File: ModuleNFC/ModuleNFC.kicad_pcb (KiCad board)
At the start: 2 copper layers, 40 parts, among them J1 Conn_01x10_Male, J2 Conn_01x04_Male, J3 Conn_01x08_Male, J4 Conn_Coaxial, Q1 2N7002DM, SW1 SW_DIP_x02, U1 PN5321A3HN_C1xx, Y1 27.12MHz

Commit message: Esquemático y PCB versión 1
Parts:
- Y1: footprint Crystal:Crystal_SMD_0603-4Pin_6.0x3.5mm -> Crystal:Crystal_SMD_0603-2Pin_6.0x3.5mm
- moved C1 70.3 mm to (188.8, 64.2), turned to 180 degrees
- moved J4 63.2 mm to (213.5, 77.0)
- moved J3 61.6 mm to (182.9, 59.5), turned to 90 degrees
- moved C8 56.9 mm to (182.5, 72.9), turned to 90 degrees
- moved C13 56.3 mm to (206.5, 79.5), turned to 270 degrees
- moved L1 56.2 mm to (202.0, 80.5), turned to 180 degrees
- moved C9 56.1 mm to (191.5, 82.0), turned to 270 degrees
- moved C7 55.1 mm to (194.0, 79.0)
- moved C5 54.9 mm to (194.0, 75.0)
- moved C18 54.7 mm to (197.8, 70.2), turned to 270 degrees
- moved C10 54.3 mm to (193.5, 82.0), turned to 270 degrees
- moved R6 54.2 mm to (193.9, 70.2), turned to 270 degrees
- moved U1 50.2 mm to (187.0, 76.5), turned to 180 degrees
- moved C11 48.4 mm to (201.0, 77.0), turned to 90 degrees
- moved R7 48.0 mm to (199.7, 70.2), turned to 270 degrees
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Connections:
- J3 pad 1: /RSTOUTN -> Net-(J3-Pad1)
- J3 pad 3: GND -> Net-(J3-Pad3)
- J3 pad 4: +3V3 -> Net-(J3-Pad4)
- J3 pad 5: Net-(J3-Pad5) -> +3V3
- J3 pad 6: Net-(J3-Pad6) -> GND
- J3 pad 8: Net-(J3-Pad8) -> /RSTOUTN
- R10 pad 1: Net-(J3-Pad6) -> Net-(J3-Pad3)
- R11 pad 1: Net-(J3-Pad5) -> Net-(J3-Pad4)
- R12 pad 1: Net-(J3-Pad2) -> Net-(J3-Pad7)
- R8 pad 1: Net-(J3-Pad8) -> Net-(J3-Pad1)
- R9 pad 1: Net-(J3-Pad7) -> Net-(J3-Pad2)
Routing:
- net GND: track 0.00 -> 217.3 mm, vias 0 -> 5
- net +3V3: track 0.00 -> 148.3 mm, vias 0 -> 3
- net Net-(R1-Pad1): track 0.00 -> 56.6 mm, vias 0 -> 2
- net Net-(R2-Pad1): track 0.00 -> 43.3 mm, vias 0 -> 2
- net /MOSI_SDA_TX: track 0.00 -> 33.3 mm, vias 0 -> 3
- net /RSTOUTN: track 0.00 -> 29.7 mm, vias 0 -> 2
- net /NSS_SCL_RX: track 0.00 -> 28.7 mm, vias 0 -> 2
- net /AUX1: track 0.00 -> 28.2 mm, vias 0 -> 1
- net /AUX2: track 0.00 -> 23.7 mm, vias 0 -> 1
- net /SCK: track 0.00 -> 18.2 mm, vias 0 -> 2
- net Net-(C11-Pad1): track 0.00 -> 17.1 mm
- net /MISO: track 0.00 -> 17.0 mm, vias 0 -> 2
- net Net-(C18-Pad2): track 0.00 -> 16.6 mm
- net /DBG_RX: track 0.00 -> 14.1 mm, vias 0 -> 1
- net Net-(J3-Pad7): track 0.00 -> 14.0 mm
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
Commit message: Board modificaed
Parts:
- moved J4 59.7 mm to (167.7, 115.3), turned to 270 degrees
- moved C15 53.7 mm to (165.7, 110.8), turned to 180 degrees
- moved C16 53.2 mm to (169.7, 110.8), turned to 180 degrees
- moved C13 50.4 mm to (165.2, 108.3), turned to 180 degrees
- moved C14 49.6 mm to (170.2, 108.3), turned to 0 degrees
- moved C18 47.0 mm to (159.0, 96.8), turned to 180 degrees
- moved C2 45.9 mm to (148.2, 96.4)
- moved C1 45.9 mm to (152.7, 92.6)
- moved C10 45.9 mm to (157.4, 110.4)
- moved C4 45.9 mm to (153.4, 110.4)
- moved C5 45.9 mm to (157.9, 103.4)
- moved C6 45.9 mm to (157.9, 105.4)
- moved C7 45.9 mm to (157.9, 107.4)
- moved C8 45.9 mm to (146.4, 101.3)
- moved C9 45.9 mm to (155.4, 110.4)
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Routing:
- net /TX2: track 12.1 -> 22.5 mm
- net Net-(C18-Pad2): track 16.6 -> 8.33 mm
- net /TX1: track 12.3 -> 16.3 mm
- net +3V3: track 148.3 -> 150.9 mm
- net GND: track 217.3 -> 214.8 mm, vias 5 -> 3
- net Net-(C17-Pad1): track 7.98 -> 9.91 mm
- net Net-(C11-Pad1): track 17.1 -> 15.8 mm
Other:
- board outline added: 52 x 39 mm
- board text added: "KiCad E.D.A"

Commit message: Added dimensions
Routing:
- net GND: track 214.8 -> 212.0 mm

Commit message: Added comment at margin with parameters of PCB
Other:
- board text added: "* No se tiene restricciones sobre el tamaño de pistas. * Se utilizo las capacidades de fabricación nacional (Mayer). * La capacidad de Mayer planteada para este módulo fue 10 mils * La grilla utilizada para acomodar componente cómo primera aproximación fue 1mm * La grilla utilizada para routear las pistas varió entre 0.25 a 0.1mm"

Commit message: Add model 3D of PN532
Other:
- board text added: "KiCad E.D.A IND. ARG"
- board text added: "V1"
- board text removed: "KiCad E.D.A"

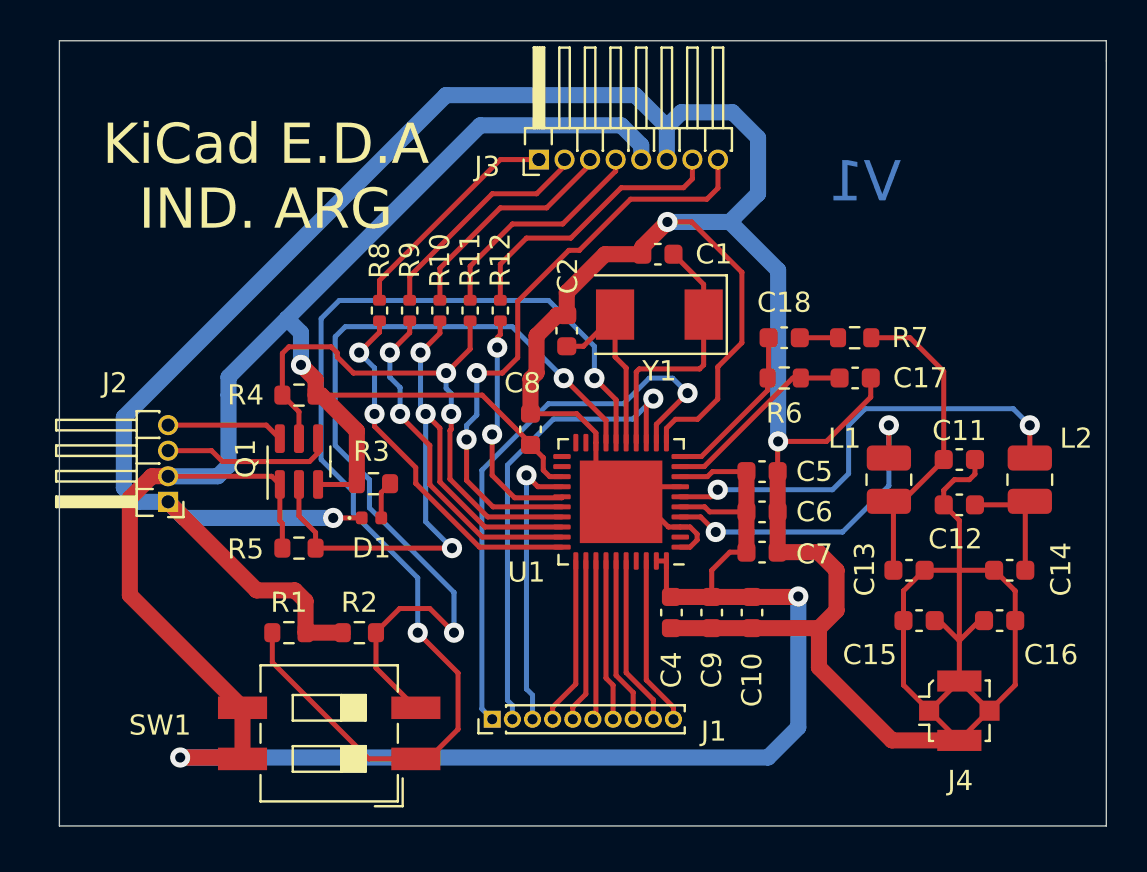
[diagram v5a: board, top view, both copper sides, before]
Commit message: Modification on PCB and Schematic on base of correction
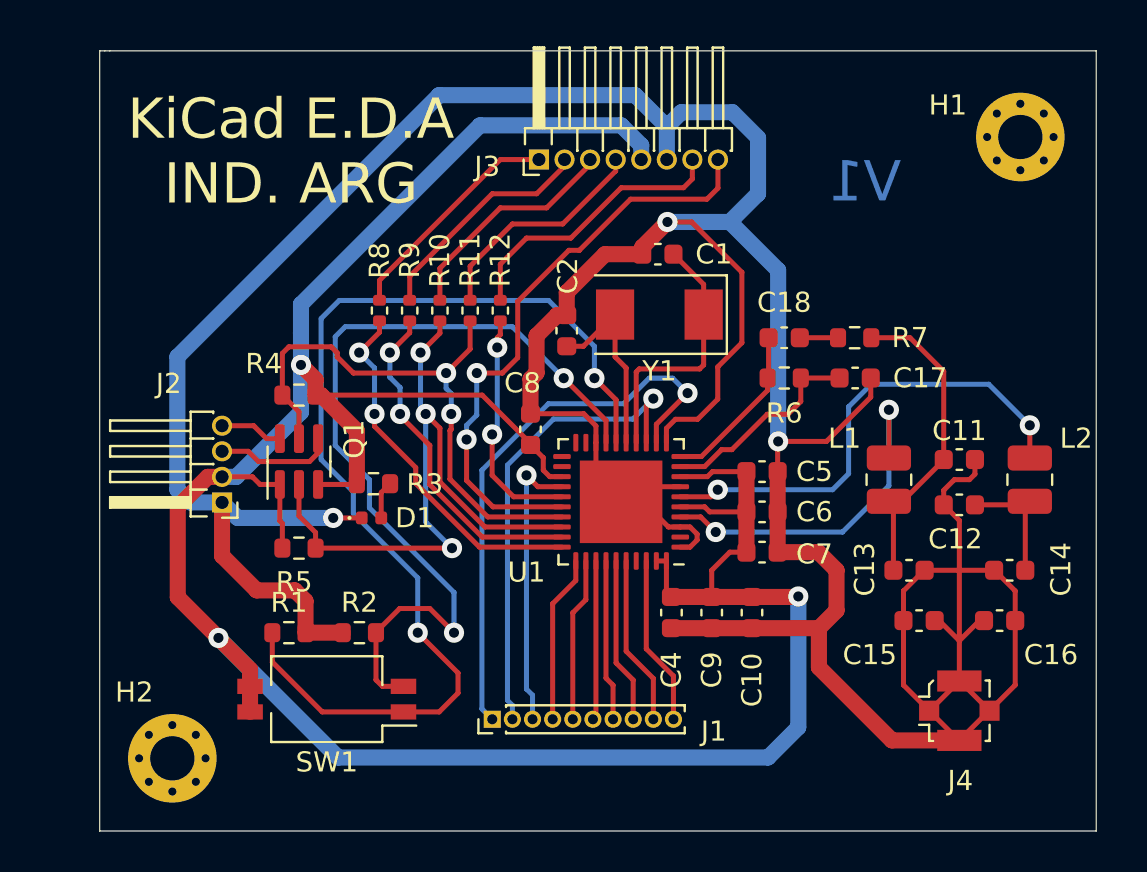
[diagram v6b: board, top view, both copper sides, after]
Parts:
- added H1: MountingHole, MountingHole:MountingHole_2.2mm_M2_Pad_Via, F.Cu at (170.7, 86.8)
- added H2: MountingHole, MountingHole:MountingHole_2.2mm_M2_Pad_Via, F.Cu at (128.6, 117.6)
- D1: value BLUE -> Led blue
- SW1: footprint Button_Switch_SMD:SW_DIP_SPSTx02_Slide_6.7x6.64mm_W8.61mm_P2.54mm_LowProfile -> Button_Switch_SMD:SW_DIP_SPSTx02_Slide_KingTek_DSHP02TS_W7.62mm_P1.27mm
- moved J2 2.68 mm to (131.1, 104.9)
- moved SW1 1.70 mm to (136.3, 114.7)
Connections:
- net /TX1 renamed Net-(L1-Pad2)
- net /TX2 renamed Net-(L2-Pad2)
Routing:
- net +3V3: track 150.9 -> 137.8 mm
- net GND: track 212.0 -> 207.6 mm
- net Net-(R1-Pad1): track 56.6 -> 53.6 mm
- net /SCL: track 5.83 -> 3.14 mm
- net /SDA: track 8.56 -> 5.87 mm
- net Net-(L2-Pad2): track 22.5 -> 24.1 mm
- net Net-(L1-Pad2): track 16.3 -> 17.8 mm
- net Net-(R2-Pad1): track 43.3 -> 42.6 mm
- net Net-(C17-Pad1): track 9.91 -> 10.6 mm
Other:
- board size 52 x 39 mm -> 49.5 x 38.8 mm
- board text added: "* No se tiene restricciones sobre el tamaño de pistas. * Se utilizo las capacidades de fabricación nacional (Mayer). * La capacidad de Mayer planteada para este módulo fue 10 mils * La grilla utilizada para acomodar componente cómo primera aproximación fue 1mm * La grilla utilizada para routear las pistas fue 0.1mm"
- board text removed: "* No se tiene restricciones sobre el tamaño de pistas. * Se utilizo las capacidades de fabricación nacional (Mayer). * La capacidad de Mayer planteada para este módulo fue 10 mils * La grilla utilizada para acomodar componente cómo primera aproximación fue 1mm * La grilla utilizada para routear las pistas varió entre 0.25 a 0.1mm"

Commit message: All modification with correction
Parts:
- added FID1: Fiducial, Fiducial:Fiducial_1mm_Mask2mm, F.Cu at (128.0, 119.1)
- added FID2: Fiducial, Fiducial:Fiducial_1mm_Mask2mm, F.Cu at (172.2, 119.1)
- added FID3: Fiducial, Fiducial:Fiducial_1mm_Mask2mm, F.Cu at (172.2, 85.6)
- C1, C10, C11, C12, C13, C14, C15, C16, C17, C18, C2, C4, C5, C6, C7, C8, C9: footprint Capacitor_SMD:C_0603_1608Metric -> Capacitor_SMD:C_0805_2012Metric
- D1: footprint LED_SMD:LED_0402_1005Metric -> LED_SMD:LED_0603_1608Metric
- R1, R2, R3, R4, R5, R6, R7: footprint Resistor_SMD:R_0603_1608Metric -> Resistor_SMD:R_0805_2012Metric
- R10, R11, R12, R8, R9: footprint Resistor_SMD:R_0402_1005Metric -> Resistor_SMD:R_0805_2012Metric
- moved H2 31.3 mm to (130.0, 86.4)
- moved H1 28.4 mm to (168.7, 115.1)
- moved J4 11.2 mm to (171.5, 104.7), turned to 0 degrees
- moved C18 11.1 mm to (169.8, 94.4), turned to 270 degrees
- moved C16 10.2 mm to (170.5, 100.6)
- moved L2 7.78 mm to (163.9, 101.1), turned to 180 degrees
- moved C1 6.96 mm to (159.5, 94.2), turned to 90 degrees
- moved C14 6.31 mm to (167.5, 102.6), turned to 90 degrees
- moved R6 5.58 mm to (162.5, 94.4), turned to 270 degrees
- moved C10 5.55 mm to (162.4, 112.8)
- moved C11 5.44 mm to (162.6, 104.7), turned to 90 degrees
- moved R7 5.34 mm to (167.3, 94.4), turned to 270 degrees
- moved C15 5.24 mm to (170.5, 108.7), turned to 0 degrees
- moved C9 5.10 mm to (159.9, 112.8)
- moved C17 4.96 mm to (164.9, 94.4), turned to 90 degrees
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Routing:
- net GND: track 207.6 -> 102.2 mm, vias 3 -> 11
- net +3V3: track 137.8 -> 46.1 mm
- net Net-(C18-Pad2): track 8.33 -> 30.9 mm
- net Net-(R1-Pad1): track 53.6 -> 38.9 mm
- net Net-(C11-Pad1): track 15.8 -> 29.0 mm, vias 0 -> 2
- net Net-(L2-Pad2): track 24.1 -> 10.9 mm, vias 2 -> 0
- net Net-(R2-Pad1): track 42.6 -> 29.9 mm
- net /MOSI_SDA_TX: track 33.5 -> 41.6 mm
- net Net-(L1-Pad2): track 17.8 -> 10.3 mm, vias 2 -> 0
- net /AUX1: track 28.2 -> 34.7 mm
- net /AUX2: track 23.7 -> 30.1 mm
- net /SCK: track 18.2 -> 23.8 mm
- net /MISO: track 17.0 -> 22.1 mm
- net /NSS_SCL_RX: track 28.7 -> 33.5 mm
- net /IRQ: track 11.8 -> 16.1 mm
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- added copper zone on F.Cu, net +3V3
- added copper zone on B.Cu, net GND
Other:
- board size 49.5 x 38.8 mm -> 48.8 x 38.8 mm
- net class Default: clearance 0.2 -> 0.25
- rule trace_clearance: 0.2 -> 0.25
- board text added: "* Las restricciones para el ancho de las pistas son los utilizados por fabricantes de industria nacional. * Se utilizo las capacidades de fabricación nacional (Mayer). * La capacidad de Mayer planteada para este módulo fue 10 mils * La grilla utilizada para acomodar componente cómo primera aproximación fue 1mm * La grilla utilizada para routear las pistas fue 0.1mm * El módelo 3D de Q1 utilizado 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"
- board text removed: "* No se tiene restricciones sobre el tamaño de pistas. * Se utilizo las capacidades de fabricación nacional (Mayer). * La capacidad de Mayer planteada para este módulo fue 10 mils * La grilla utilizada para acomodar componente cómo primera aproximación fue 1mm * La grilla utilizada para routear las pistas fue 0.1mm"

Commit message: Export model 3D
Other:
- net class Default: clearance 0.25 -> 0.2
- rule trace_clearance: 0.25 -> 0.2
